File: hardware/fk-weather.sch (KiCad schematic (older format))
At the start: 67 parts, among them J1 RJ11-6, J2 MICRO-USB, J3 RJ11-6, J4 CONN-HDR-1x19, J5 CONN-HDR-1x19, J6 CONN-HDR-2x5, M1 MOUNT_HOLE, M2 MOUNT_HOLE, M3 MOUNT_HOLE, M4 MOUNT_HOLE, M5 FIDUCIAL, M6 FIDUCIAL, P1 CONN-HDR-MODULE, Q1 2N7002LT1G, SW1 SPNO, U1 ATSAMD21G18A-AU, U2 BQ24074RGTT, U4 MCP1700T-3302E/MB, Y1 FC-135

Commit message: Starting on the basic sensor module board. Just IC stuff.
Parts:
- removed C10, C17: 4.7uF 10V X5R, RocketScreamKicadLibrary:CAP-0402, symbol CAPACITOR-CERAMIC
- removed C15, C19: 1uF 10V X5R, RocketScreamKicadLibrary:CAP-0402, symbol CAPACITOR-CERAMIC
- removed C18: 4.7nF 25V X7R, RocketScreamKicadLibrary:CAP-0402, symbol CAPACITOR-CERAMIC
- removed C9: 1uF 50V X5R, RocketScreamKicadLibrary:CAP-0603, symbol CAPACITOR-CERAMIC
- removed D10, D5, D6, D7, D8, D9: BAS16, RocketScreamKicadLibrary:DIO-0603, symbol D
- removed D2: LED-DUAL, RocketScreamKicadLibrary:LED-1615, symbol LED-DUAL
- removed D3: PRTR5V0U2X, RocketScreamKicadLibrary:SOT-143B, symbol PRTR5V0U2X
- removed D4: PMEG3020CPA, RocketScreamKicadLibrary:SOT-1016, symbol DIODE_DUAL_Schottky
- removed F1: MF-PSMF050X-2, RocketScreamKicadLibrary:MF-PSMF020X, symbol FUSE
- removed J1, J3: RJ11-6, fk-weather:molex_95501-2641, symbol RJ11-6
- removed J2: MICRO-USB, RocketScreamKicadLibrary:MICRO-USB, symbol MICRO-USB
- removed J4, J5: CONN-HDR-1x19, RocketScreamKicadLibrary:HDR_1x19_Pitch2.54mm_WithoutSilk, symbol CONN-HDR-1x19
- removed L1: BKP1005TS121-T, RocketScreamKicadLibrary:IND-0402, symbol INDUCTOR
- removed M5, M6: FIDUCIAL, RocketScreamKicadLibrary:FIDUCIAL-1MM, symbol FIDUCIAL
- removed P1: CONN-HDR-MODULE, fk-core-mini-ultra-pro:Socket_Strip_Straight_1x05_Pitch2.54mm, symbol CONN_01X05
- removed R10, R13: 2K2, RocketScreamKicadLibrary:RES-0402, symbol RESISTOR
- removed R11: 100K, RocketScreamKicadLibrary:RES-0402, symbol RESISTOR
- removed R12, R8: 10K, RocketScreamKicadLibrary:RES-0402, symbol RESISTOR
- removed R14, R15, R16, R17, R19, R20: 1K, RocketScreamKicadLibrary:RES-0603, symbol RESISTOR
- removed R18: 4.7K, RocketScreamKicadLibrary:RES-0603, symbol RESISTOR
- removed R6: 1K18, RocketScreamKicadLibrary:RES-0402, symbol RESISTOR
- removed R7: 46K4, RocketScreamKicadLibrary:RES-0402, symbol RESISTOR
- removed R9: 2K94, RocketScreamKicadLibrary:RES-0402, symbol RESISTOR
- removed U2: BQ24074RGTT, RocketScreamKicadLibrary:QFN-16_3x3mm, symbol BQ24074
- removed U4: MCP1700T-3302E/MB, RocketScreamKicadLibrary:SOT-89, symbol MCP1700T-XXX2E
- added C101: 1uF, Capacitors_SMD:C_0603_HandSoldering, symbol CAPACITOR-CERAMIC
- added C102, C103, C106, C108, C109: 100nF, Capacitors_SMD:C_0603_HandSoldering, symbol CAPACITOR-CERAMIC
- added C104: 10uF, Capacitors_SMD:C_0603_HandSoldering, symbol CAPACITOR-CERAMIC
- added C105, C107: 22pF, Capacitors_SMD:C_0603_HandSoldering, symbol CAPACITOR-CERAMIC
- added D2: Yellow, RocketScreamKicadLibrary:LED-0603, symbol LED-SINGLE
- added D3: Blue, RocketScreamKicadLibrary:LED-0603, symbol LED-SINGLE
- added P101: CONN_01X05, Socket_Strips:Socket_Strip_Straight_1x05_Pitch2.54mm, symbol CONN_01X05
- added Q2, Q3: 2N7002LT1G, RocketScreamKicadLibrary:SOT-23, symbol MOSFET-N
- added R101, R102, R103: 10K, Resistors_SMD:R_0603_HandSoldering, symbol RESISTOR
- added U101: TSL2591, Housings_DFN_QFN:DFN-6-1.3x1.2mm_Pitch0.4mm, symbol TSL2591
- added U102: MPL3115A2, Housings_DFN_QFN:DFN-8_2x2mm_Pitch0.5mm, symbol MPL3115A2
- added U103: BNO055, conservify:BNO055, symbol BNO055-RESCUE-fk-weather
- added U104: SHT31, Housings_DFN_QFN:DFN-8_2x2mm_Pitch0.5mm, symbol SHT31
- added Y101: FC-135, RocketScreamKicadLibrary:ABS07, symbol CRYSTAL
- C1, C2: footprint RocketScreamKicadLibrary:CAP-0402 -> Capacitors_SMD:C_0603_HandSoldering; spn1 (none) -> 581-06035A180J; supplier1 (none) -> mouser
- C14: footprint RocketScreamKicadLibrary:CAP-0402 -> Capacitors_SMD:C_0603_HandSoldering; spn1 (none) -> 581-0603ZD475MAT2A; supplier1 (none) -> mouser
- C3, C4, C6, C7, C8: footprint RocketScreamKicadLibrary:CAP-0402 -> Capacitors_SMD:C_0603_HandSoldering; spn1 (none) -> 81-GRM39X104K50D; supplier1 (none) -> mouser
- C5: footprint RocketScreamKicadLibrary:CAP-0402 -> Capacitors_SMD:C_0603_HandSoldering; spn1 (none) -> 581-0603YD105K; supplier1 (none) -> mouser
- D1: spn1 (none) -> 859-LTST-C190KFKT; supplier1 (none) -> mouser
- J6: footprint RocketScreamKicadLibrary:HDR_2x5_Pitch1.27mm -> Socket_Strips:Socket_Strip_Straight_2x05_Pitch1.27mm_SMD; spn1 (none) -> 649-202112100010C4LF; supplier1 (none) -> mouser
- L2: spn1 (none) -> 963-BKP1608HS121-T; supplier1 (none) -> mouser
- Q1: spn1 (none) -> 863-2N7002LT1G; supplier1 (none) -> mouser
- R1: value 2K2 -> 2k2; footprint RocketScreamKicadLibrary:RES-0402 -> RocketScreamKicadLibrary:RES-0603; spn1 (none) -> 603-RC0603FR-072K2L; supplier1 (none) -> mouser
- R2: footprint RocketScreamKicadLibrary:RES-0402 -> Resistors_SMD:R_0603_HandSoldering; spn1 (none) -> 603-RC0603FR-07330RL; supplier1 (none) -> mouser
- R3: value 330R -> 2k2; footprint RocketScreamKicadLibrary:RES-0402 -> RocketScreamKicadLibrary:RES-0603; spn1 (none) -> 603-RC0603FR-072K2L; supplier1 (none) -> mouser
- R4: footprint RocketScreamKicadLibrary:RES-0402 -> Resistors_SMD:R_0603_HandSoldering; spn1 (none) -> 603-RC0603FR-0710KL; supplier1 (none) -> mouser
- R5: value 1M -> 2k2; footprint RocketScreamKicadLibrary:RES-0402 -> RocketScreamKicadLibrary:RES-0603; spn1 (none) -> 603-RC0603FR-072K2L; supplier1 (none) -> mouser
- U1: spn1 (none) -> 556-ATSAMD21G18A-AU; supplier1 (none) -> mouser
- Y1: spn1 (none) -> 732-FC135-32.76KAA3; supplier1 (none) -> mouser
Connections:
- net labels removed: 5V0, CHG, D13, PG, RAIN, RAIN2, RAIN5, SD_CS, VBAT, VBUS, VEXT, VIN, VUSB, WIND_DIR, WIND_SPEED
- wire segments 273 -> 187
- no-connect marks 14 -> 13
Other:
- note removed: "1. All capacitors are NP0/COG 50V unless specified.\n2. All resistors are 62.5mW 1% unless specified."
- note removed: "100mA"
- note removed: "2.54 mm (0.1") breakout"
- note removed: "500mA"
- note removed: "BREAKOUT"
- note removed: "EN2 EN1"
- note removed: "FIDUCIALS"
- note removed: "HI HI"
- note removed: "HI LOW"
- note removed: "I-INPUT LIMIT"
- note removed: "LED"
- note removed: "LOW HI"
- note removed: "LOW LOW"
- note removed: "MCU"
- note removed: "MOUNTING"
- note removed: "NOTES"
- note removed: "POWER MANAGEMENT"
- note removed: "SWD/JTAG"
- note removed: "Set by R6:1.3A"
- note removed: "Standby"
- note removed: "USB-DEVICE"
- note removed: "VIN:5-10.5V\n(OVP up to 28V)"
- moved on the sheet: J6, M1, M2, M3, M4

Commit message: Adding pull ups, fixing the outline. Plotting.
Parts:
- added R6, R7: 4.7k, Resistors_SMD:R_0603_HandSoldering, symbol RESISTOR
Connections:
- wire segments 187 -> 191

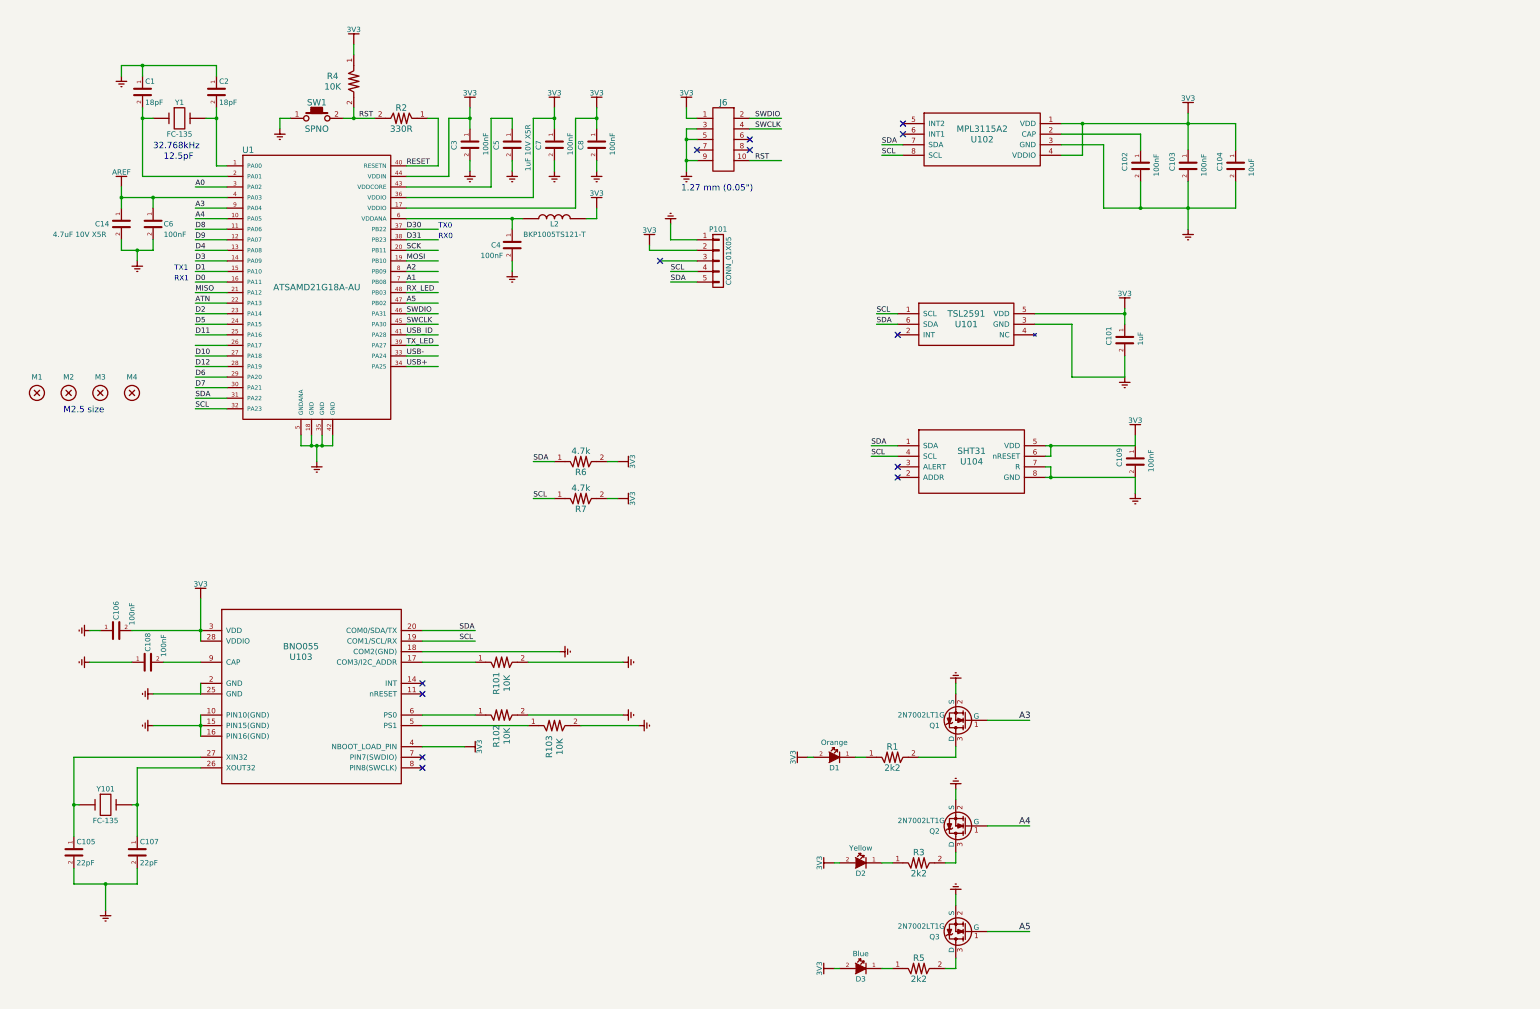
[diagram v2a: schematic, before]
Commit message: Adding USB connector and 3v3 regulator.
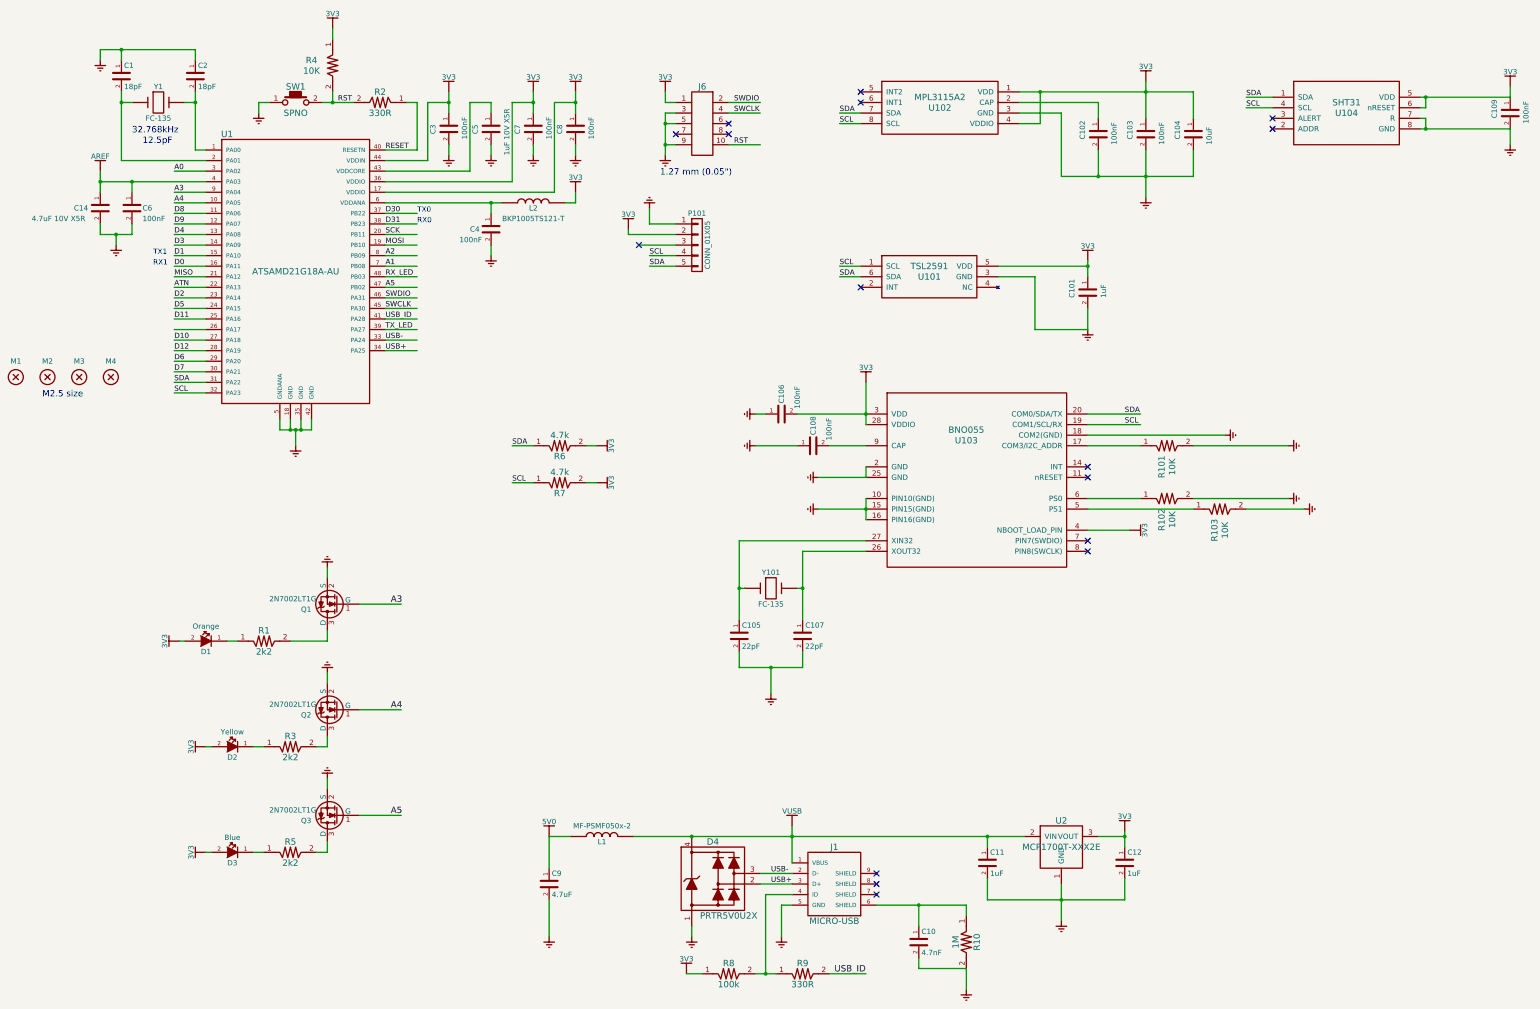
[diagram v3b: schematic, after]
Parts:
- added C10: 4.7nF, Capacitors_SMD:C_0603_HandSoldering, symbol CAPACITOR-CERAMIC
- added C11, C12: 1uF, Capacitors_SMD:C_0603_HandSoldering, symbol CAPACITOR-CERAMIC
- added C9: 4.7uF, Capacitors_SMD:C_0603_HandSoldering, symbol CAPACITOR-CERAMIC
- added D4: PRTR5V0U2X, RocketScreamKicadLibrary:SOT-143B, symbol PRTR5V0U2X
- added J1: MICRO-USB, RocketScreamKicadLibrary:MICRO-USB, symbol MICRO-USB
- added L1: MF-PSMF050x-2, RocketScreamKicadLibrary:IND-0603, symbol INDUCTOR
- added R10: 1M, Resistors_SMD:R_0603_HandSoldering, symbol RESISTOR
- added R8: 100k, Resistors_SMD:R_0603_HandSoldering, symbol RESISTOR
- added R9: 330R, Resistors_SMD:R_0603_HandSoldering, symbol RESISTOR
- added U2: MCP1700T-XXX2E, RocketScreamKicadLibrary:SOT-89, symbol MCP1700T-XXX2E
- R1, R3, R5: footprint RocketScreamKicadLibrary:RES-0603 -> Resistors_SMD:R_0603_HandSoldering
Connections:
- net labels added: 5V0, VUSB
- wire segments 191 -> 219
- no-connect marks 13 -> 16
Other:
- moved on the sheet: C1, C101, C102, C103, C104, C105, C106, C107, C108, C109, C14, C2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

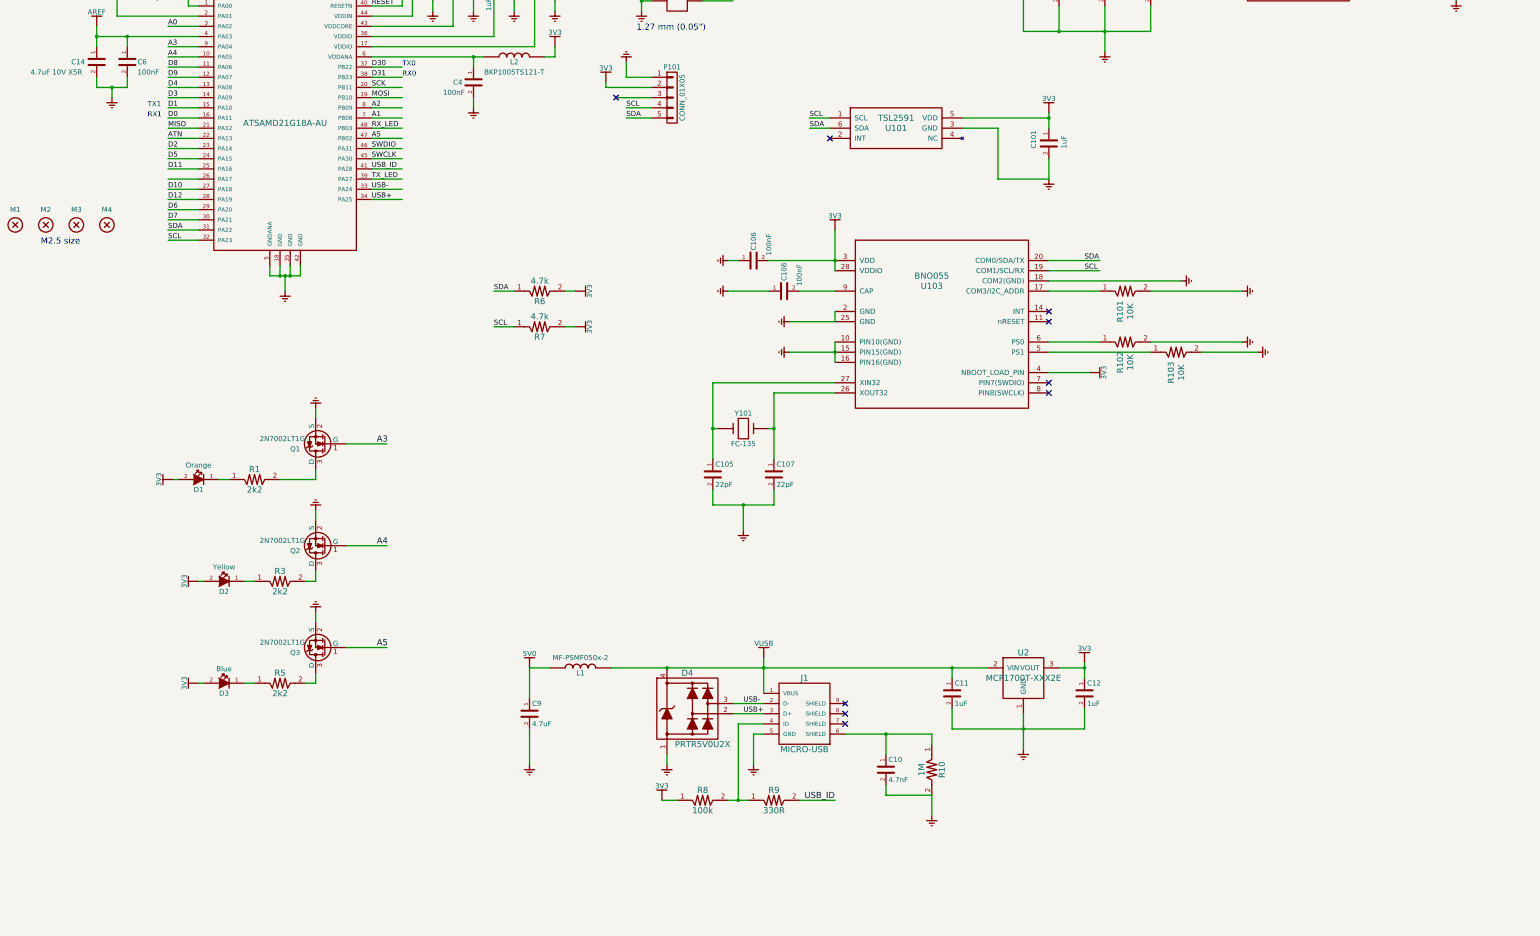
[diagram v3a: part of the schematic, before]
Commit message: Adding MAX4466.
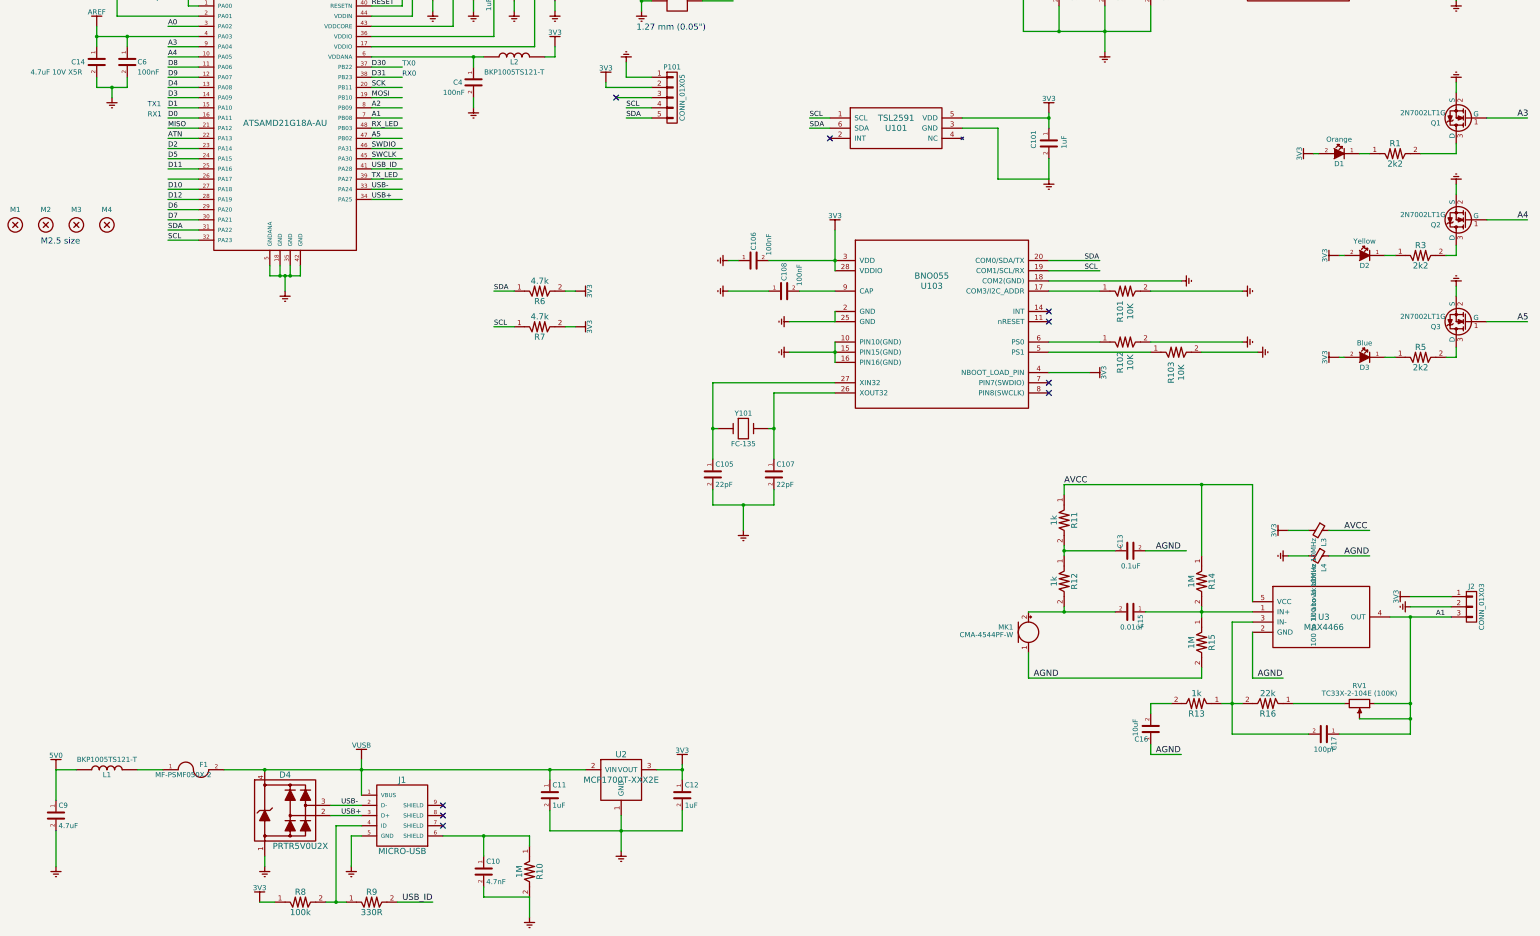
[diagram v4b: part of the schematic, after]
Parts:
- added C13: 0.1uF, Capacitors_SMD:C_0603_HandSoldering, symbol CAPACITOR-CERAMIC
- added C15: 0.01uF, Capacitors_SMD:C_0603_HandSoldering, symbol CAPACITOR-CERAMIC
- added C16: 10uF, Capacitors_SMD:C_0603_HandSoldering, symbol CAPACITOR-CERAMIC
- added C17: 100pF, Capacitors_SMD:C_0603_HandSoldering, symbol CAPACITOR-CERAMIC
- added F1: MF-PSMF050X-2, RocketScreamKicadLibrary:MF-PSMF020X, symbol FUSE
- added J2: CONN_01X03, Socket_Strips:Socket_Strip_Straight_1x03_Pitch2.54mm, symbol CONN_01X03
- added L3, L4: 100 to 1k above 10MHz, Resistors_SMD:R_0603_HandSoldering, symbol Ferrite_Bead_Small
- added MK1: CMA-4544PF-W, Socket_Strips:Socket_Strip_Angled_1x02_Pitch2.54mm, symbol Microphone
- added R11, R12, R13: 1k, Resistors_SMD:R_0603_HandSoldering, symbol RESISTOR
- added R14, R15: 1M, Resistors_SMD:R_0603_HandSoldering, symbol RESISTOR
- added R16: 22k, Resistors_SMD:R_0603_HandSoldering, symbol RESISTOR
- added RV1: TC33X-2-104E (100K), conservify:BOURNS-TC33X-2, symbol POT
- added U3: MAX4466, conservify:SC70-5, symbol MAX4466
- C10: spn1 (none) -> 603-AC603KRX7R8BB472; supplier1 (none) -> mouser
- C11, C12: spn1 (none) -> 581-0603YD105K; supplier1 (none) -> mouser
- C9: spn1 (none) -> 581-0603ZD475MAT2A; supplier1 (none) -> mouser
- D4: spn1 (none) -> 771-PRTR5V0U2X-T/R; supplier1 (none) -> mouser
- L1: value MF-PSMF050x-2 -> BKP1005TS121-T; spn1 (none) -> 963-BKP1608HS121-T; supplier1 (none) -> mouser
- R10: spn1 (none) -> 603-RC0603FR-071ML; supplier1 (none) -> mouser
- R8: spn1 (none) -> 603-RC0603FR-07100KL; supplier1 (none) -> mouser
- R9: spn1 (none) -> 603-RC0603FR-07330RL; supplier1 (none) -> mouser
- U2: spn1 (none) -> 579-MCP1700T3302E/MB; supplier1 (none) -> mouser
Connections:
- net labels added: AGND, AVCC
- wire segments 219 -> 256
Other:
- moved on the sheet: C10, C11, C12, C9, D1, D2, D3, D4, J1, L1, Q1, Q2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

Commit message: Fix part for ferrite beads, replot.
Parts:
- L3, L4: spn1 732-1592-1-ND -> 710-742792641
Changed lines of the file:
@@
 F 2 "Resistors_SMD:R_0603_HandSoldering" V 13580 7100 50  0001 C CNN
 F 3 "" H 13650 7100 50  0001 C CNN
-F 4 "732-1592-1-ND" H 0   0   50  0001 C CNN "spn1"
+F 4 "710-742792641" H 0   0   50  0001 C CNN "spn1"
 F 5 "mouser" H 0   0   50  0001 C CNN "supplier1"
 	1    13650 7100
@@
 F 2 "Resistors_SMD:R_0603_HandSoldering" V 13580 7350 50  0001 C CNN
 F 3 "" H 13650 7350 50  0001 C CNN
-F 4 "732-1592-1-ND" H 0   0   50  0001 C CNN "spn1"
+F 4 "710-742792641" H 0   0   50  0001 C CNN "spn1"
 F 5 "mouser" H 0   0   50  0001 C CNN "supplier1"
 	1    13650 7350
